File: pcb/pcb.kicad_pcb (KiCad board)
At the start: 2 copper layers, 130 parts, among them J1 I2C_Data, J2 SPI_Flash, SW1 Select, SW2 Done, U1 ATmega328P-AU, U2 DessinAfficheur, Y1 16Mhz

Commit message: v2 with bom
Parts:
- moved U1 0.30 mm to (37.7, 63.8)
- moved Y1 0.20 mm to (29.6, 56.3)
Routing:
- net GND: track 76.0 -> 74.9 mm
- net Net-(U1-Pad7): track 6.68 -> 5.86 mm
- net Net-(R1-Pad1): track 25.6 -> 25.1 mm
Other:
- board outline added: 53 x 73 mm

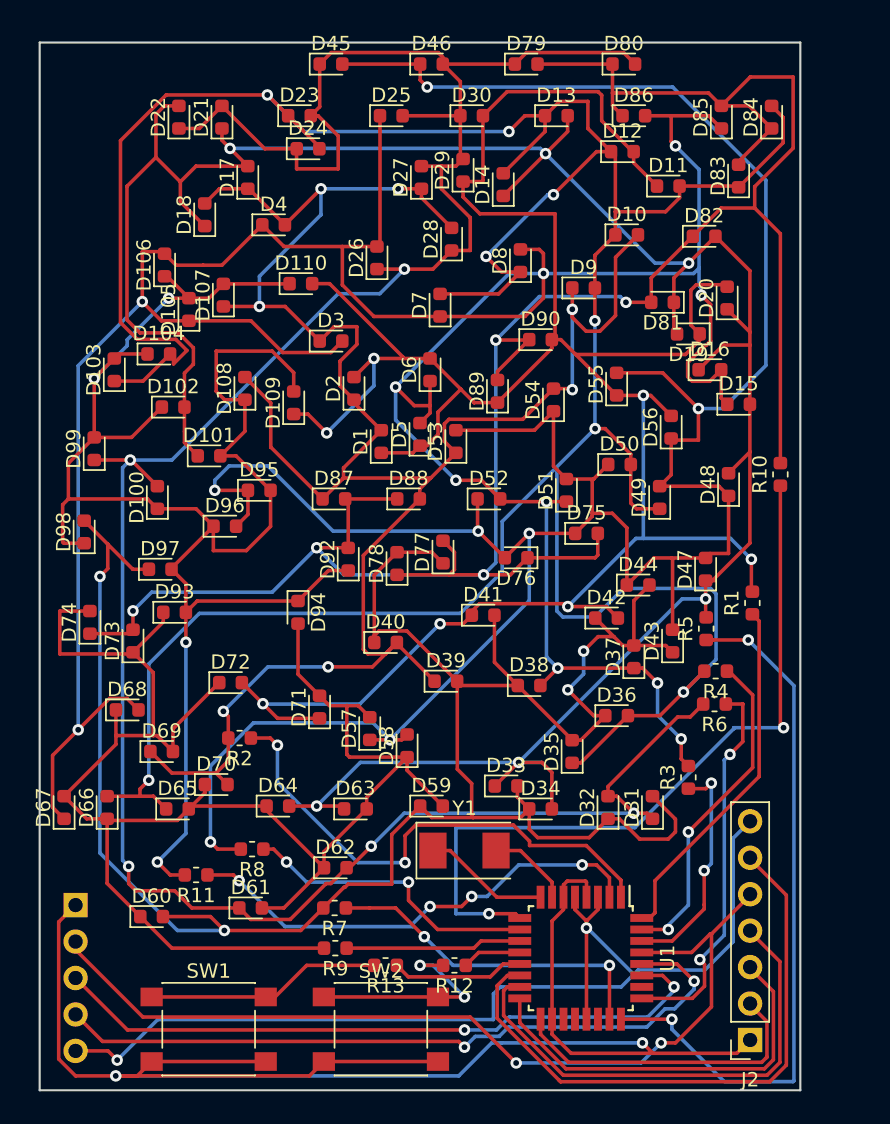
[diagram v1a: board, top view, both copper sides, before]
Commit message: clean footprints and update bom
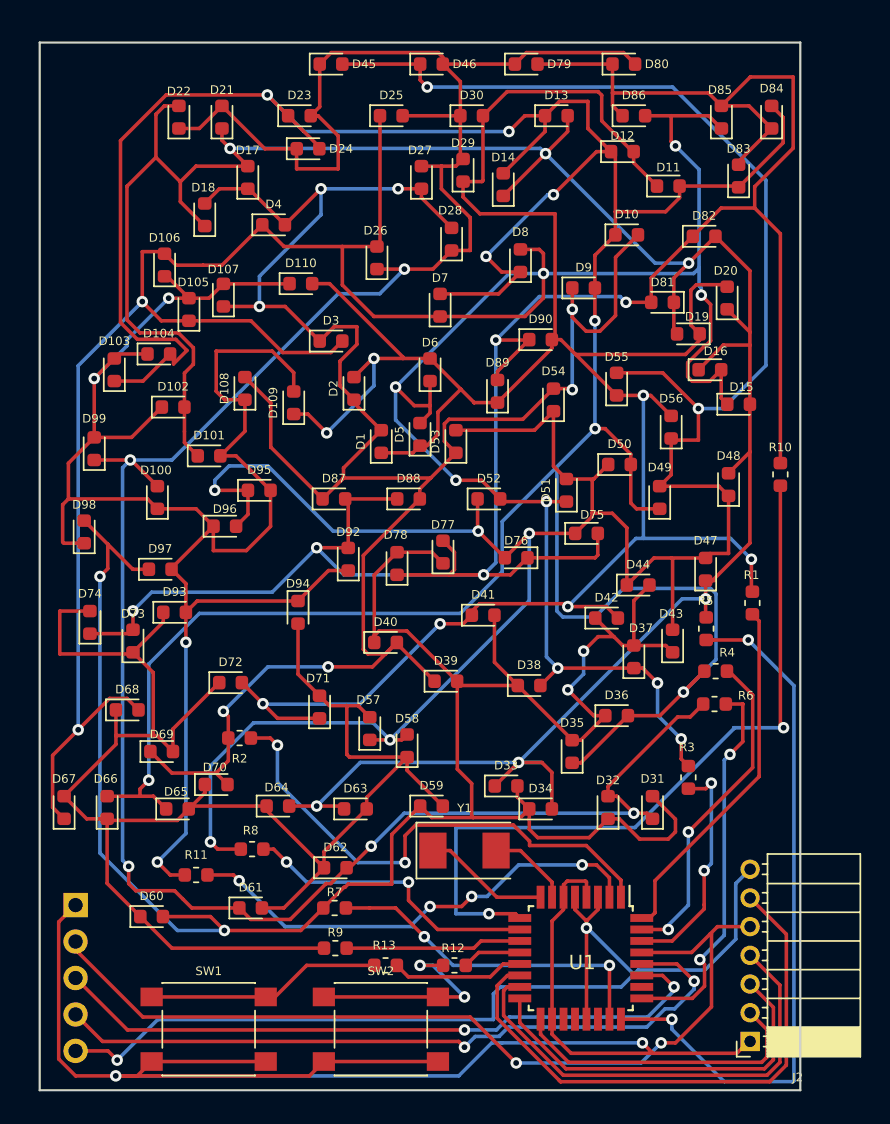
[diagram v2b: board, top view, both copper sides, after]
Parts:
- D1, D10, D100, D101, D102, D103, D104, D105, D106, D107, D108, D109, D11, D110, D12, D13, D14, D15, D16, D17, D18, D19, D2, D20, D21, D22, D23, D24, D25, D26, D27, D28, D29, D3, D30, D31, D32, D33, D34, D35, D36, D37, D38, D39, D4, D40, D41, D42, D43, D44, D45, D46, D47, D48, D49, D5, D50, D51, D52, D53, D54, D55, D56, D57, D58, D59, D6, D60, D61, D62, D63, D64, D65, D66, D67, D68, D69, D7, D70, D71, D72, D73, D74, D75, D76, D77, D78, D79, D8, D80, D81, D82, D83, D84, D85, D86, D87, D88, D89, D9, D90, D92, D93, D94, D95, D96, D97, D98, D99: footprint LED_SMD:LED_0603_1608Metric -> pasteur-lib:LED_0603_1608Metric_smallfont
- J1: footprint Connector_PinSocket_2.54mm:PinSocket_1x05_P2.54mm_Vertical -> pasteur-lib:PinSocket_1x05_P2.54mm_Vertical_smallfont
- J2: footprint Connector_PinSocket_2.54mm:PinSocket_1x07_P2.54mm_Vertical -> pasteur-lib:PinSocket_1x07_P2.00mm_Horizontal_smallfont
- R1, R10, R11, R12, R13, R2, R3, R4, R5, R6, R7, R8, R9: footprint Resistor_SMD:R_0603_1608Metric -> pasteur-lib:R_0603_1608Metric_smallfont
- SW1, SW2: footprint Button_Switch_SMD:SW_Push_1P1T_NO_6x6mm_H9.5mm -> pasteur-lib:SW_Push_1P1T_NO_6x6mm_H9.5mm_smallfont
- Y1: footprint Crystal:Crystal_SMD_0603-2Pin_6.0x3.5mm -> pasteur-lib:Crystal_SMD_0603-2Pin_6.0x3.5mm_smallfont
- moved J2 0.10 mm to (49.5, 69.6)
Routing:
- net GND: track 74.9 -> 71.5 mm
- net Net-(J2-Pad6): track 42.2 -> 39.4 mm
- net Net-(J2-Pad3): track 28.0 -> 26.9 mm
- net Net-(J2-Pad4): track 34.3 -> 33.2 mm
- net Net-(J1-Pad2): track 64.0 -> 63.2 mm
- net Net-(J2-Pad2): track 22.0 -> 21.5 mm

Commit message: add label and netlist parser
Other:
- board text added: "CLK"
- board text added: "GND"
- board text added: "MISO"
- board text added: "MOSI"
- board text added: "RST"
- board text added: "SELECT DONE"
- board text added: "SS"
- board text added: "VCC"
- board text added: "VCC RESET SDA SCL GND"

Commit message: Minor fix and prepare for release
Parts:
- removed the U2 at (26.4, 30.7) (x2)
- added U2: HotelPasteur-V4.0, pasteur-lib:DessinAfficheurV4.0, F.Cu at (26.5, 31.0)
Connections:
- U1 pad 19: Net-(U1-Pad19) -> (no net)
- U1 pad 20: Net-(U1-Pad20) -> (no net)
- U1 pad 22: Net-(U1-Pad22) -> (no net)
- U1 pad 26: Net-(U1-Pad26) -> (no net)
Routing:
- net /NL05: track 180.7 -> 178.4 mm
- net /NL04: track 237.9 -> 235.8 mm
- net /NL10: track 165.0 -> 165.6 mm
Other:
- board text added: "AG-LM-UnivRennes1"
